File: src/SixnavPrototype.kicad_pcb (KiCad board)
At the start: 2 copper layers, 66 x 114.3 mm, 35 parts, among them Q1 PT908-7C-F, Q2 PT908-7C-F, Q3 PT908-7C-F, Q4 PT908-7C-F, Q5 PT908-7C-F, Q6 PT908-7C-F, U1 Pico, U2 CD4051B

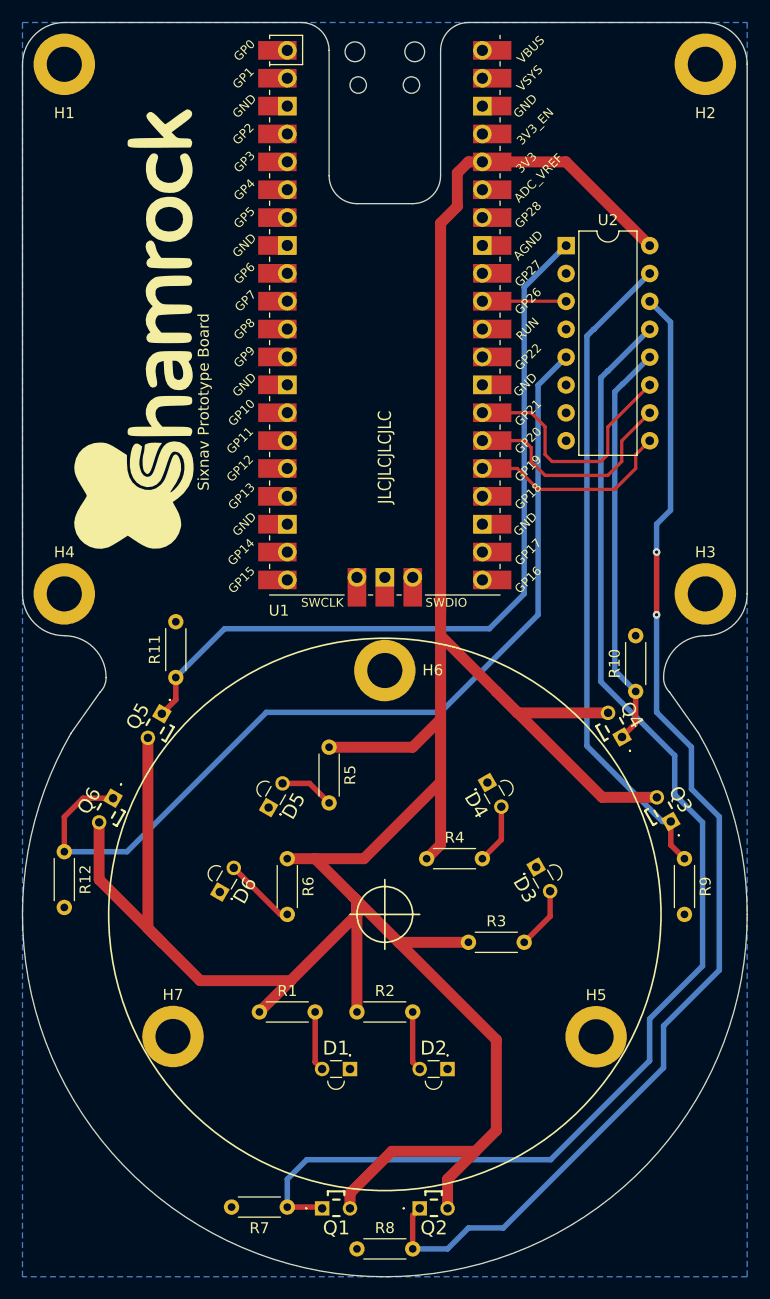
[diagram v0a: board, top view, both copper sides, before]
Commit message: Replaced symbols, footprints, models, with lib
Internal libraries also fix the reversed phototransistor issue.
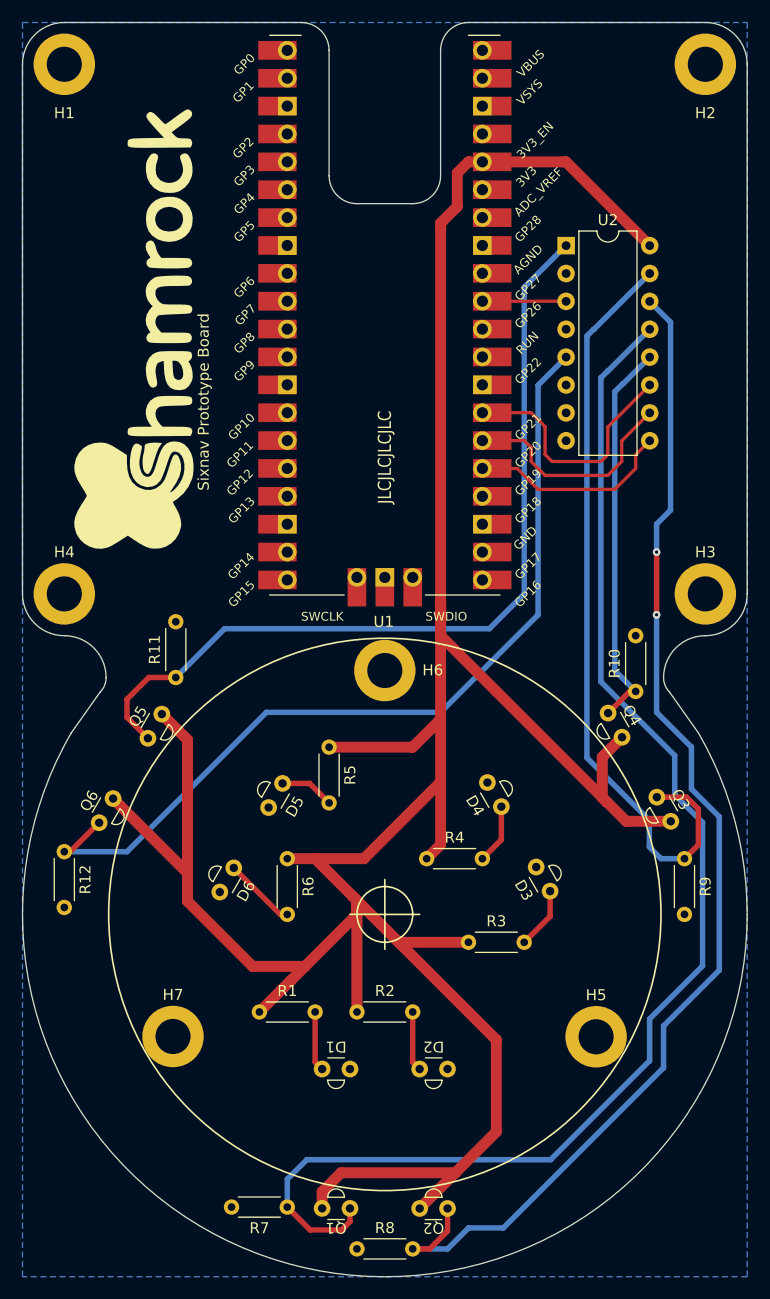
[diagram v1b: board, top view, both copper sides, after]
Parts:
- D1, D2, D3, D4, D5, D6: footprint SamacSys_Parts:IR9087CF -> LibSixnavPrototype:IR908-7C-F
- Q1, Q2, Q3, Q4, Q5, Q6: footprint SamacSys_Parts:ELPT9087C -> LibSixnavPrototype:PT908-7C-F
- U1: footprint MCU_RaspberryPi_and_Boards:RPi_Pico_SMD_TH -> LibSixnavPrototype:Raspberry Pi Pico
- moved Q5 2.57 mm to (118.1, 110.9), turned to 60 degrees
- moved Q6 2.57 mm to (113.7, 118.6), turned to 60 degrees
- moved Q3 2.55 mm to (164.5, 116.3), turned to -60 degrees
- moved Q2 2.54 mm to (145.4, 153.8), turned to 180 degrees
- moved Q1 2.54 mm to (136.5, 153.8), turned to 180 degrees
- moved Q4 2.52 mm to (160.0, 108.7), turned to -60 degrees
- moved U1 1.27 mm to (139.7, 73.7)
- turned D1 to 180 degrees
- turned D2 to 180 degrees
- turned D3 to -60 degrees
- turned D4 to -60 degrees
- turned D5 to 60 degrees
- turned D6 to 60 degrees
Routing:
- net /MUX_X2_Q3: track 59.8 -> 69.9 mm
- net /MUX_X4_Q5: track 72.1 -> 77.8 mm
- net +3.3V: track 285.4 -> 280.1 mm
- net /MUX_X0_Q1: track 117.6 -> 122.5 mm
- net /MUX_X5_Q6: track 85.0 -> 80.9 mm
- net /MUX_X1_Q2: track 109.3 -> 111.2 mm
- net /MUX_X3_Q4: track 37.3 -> 35.9 mm

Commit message: add symbols, fix LED polarity
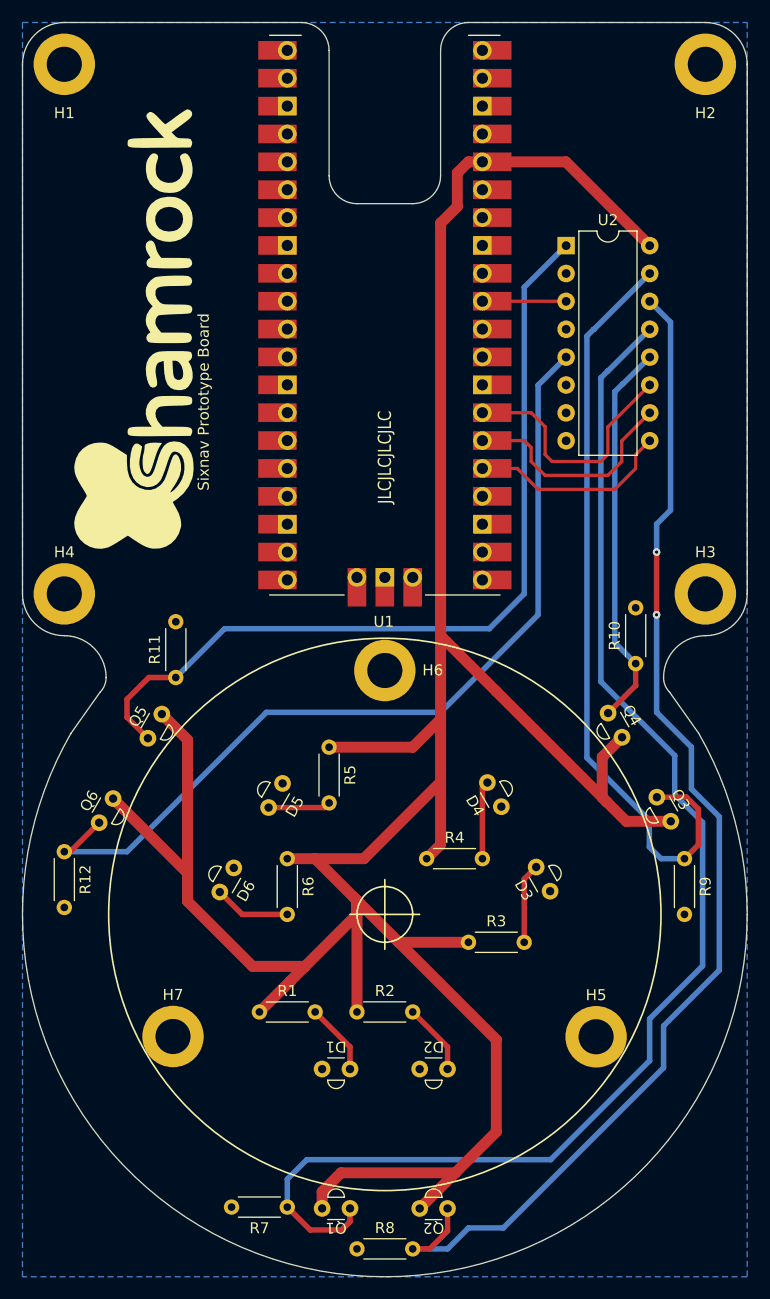
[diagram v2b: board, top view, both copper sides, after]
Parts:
- moved R10 2.54 mm to (162.6, 104.1)
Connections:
- D1 pad 1: GND -> /D1_A
- D1 pad 2: /D1_A -> GND
- D2 pad 1: GND -> /D2_A
- D2 pad 2: /D2_A -> GND
- D3 pad 1: GND -> /D3_A
- D3 pad 2: /D3_A -> GND
- D4 pad 1: GND -> /D4_A
- D4 pad 2: /D4_A -> GND
- D5 pad 1: GND -> /D5_A
- D5 pad 2: /D5_A -> GND
- D6 pad 1: GND -> /D6_A
- D6 pad 2: /D6_A -> GND
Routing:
- net /D4_A: track 5.45 -> 7.13 mm
- net /D3_A: track 5.64 -> 7.31 mm
- net /D2_A: track 5.46 -> 6.52 mm
- net /D1_A: track 5.46 -> 6.52 mm
- net /D5_A: track 4.98 -> 5.69 mm
